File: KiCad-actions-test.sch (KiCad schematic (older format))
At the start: 3 parts

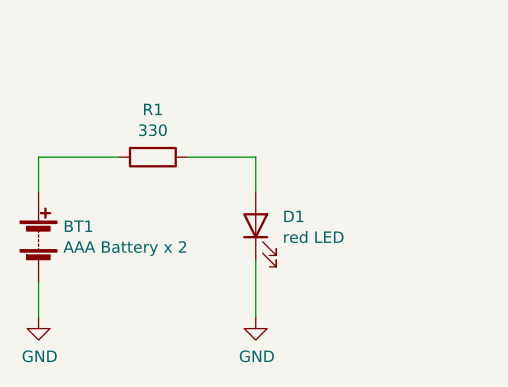
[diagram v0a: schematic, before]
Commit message: add one more led
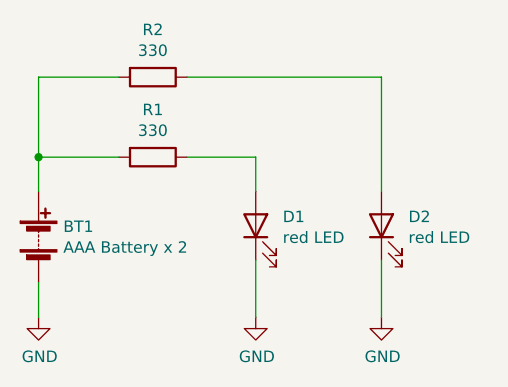
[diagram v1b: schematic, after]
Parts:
- added D2: red LED, LED_THT:LED_D5.0mm, symbol Device:LED
- added R2: 330, Resistor_THT:R_Axial_DIN0614_L14.3mm_D5.7mm_P25.40mm_Horizontal, symbol Device:R
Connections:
- net GND: now also D2.1 (K)
- net at BT1.1 (+), R1.2: now also R2.2
- new net: D2.2 (A), R2.1
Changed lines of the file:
@@
 Wire Wire Line
 	4350 3350 4350 3500
+$Comp
+L Device:LED D2
+U 1 1 5FA1681A
+P 4900 3650
+F 0 "D2" V 4939 3532 50  0000 R CNN
+F 1 "red LED" V 4848 3532 50  0000 R CNN
+F 2 "LED_THT:LED_D5.0mm" H 4900 3650 50  0001 C CNN
+F 3 "~" H 4900 3650 50  0001 C CNN
+	1    4900 3650
+	0    -1   -1   0
+$EndComp
+$Comp
+L Device:R R2
+U 1 1 5FA17217
+P 3900 3000
+F 0 "R2" V 3693 3000 50  0000 C CNN
+F 1 "330" V 3784 3000 50  0000 C CNN
+F 2 "Resistor_THT:R_Axial_DIN0614_L14.3mm_D5.7mm_P25.40mm_Horizontal" V 3830 3000 50  0001 C CNN
+F 3 "~" H 3900 3000 50  0001 C CNN
+	1    3900 3000
+	0    1    1    0
+$EndComp
+Wire Wire Line
+	3400 3350 3400 3000
+Wire Wire Line
+	3400 3000 3750 3000
+Connection ~ 3400 3350
+Wire Wire Line
+	4050 3000 4900 3000
+Wire Wire Line
+	4900 3000 4900 3500
+$Comp
+L power:GND #PWR0101
+U 1 1 5FA18561
+P 4900 4050
+F 0 "#PWR0101" H 4900 3800 50  0001 C CNN
+F 1 "GND" H 4905 3877 50  0000 C CNN
+F 2 "" H 4900 4050 50  0001 C CNN
+F 3 "" H 4900 4050 50  0001 C CNN
+	1    4900 4050
+	1    0    0    -1
+$EndComp
+Wire Wire Line
+	4900 4050 4900 3800
 $EndSCHEMATC
